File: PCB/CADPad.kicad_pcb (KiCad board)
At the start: 2 copper layers, 30 parts, among them SW1 SW_Push, SW10 RotaryEncoder_Switch, SW2 SW_Push, SW3 SW_Push, SW4 SW_Push, SW5 SW_Push, SW6 SW_Push, SW7 SW_Push, SW8 SW_Push, SW9 SW_Push, U1 XIAO-RP2040-DIP

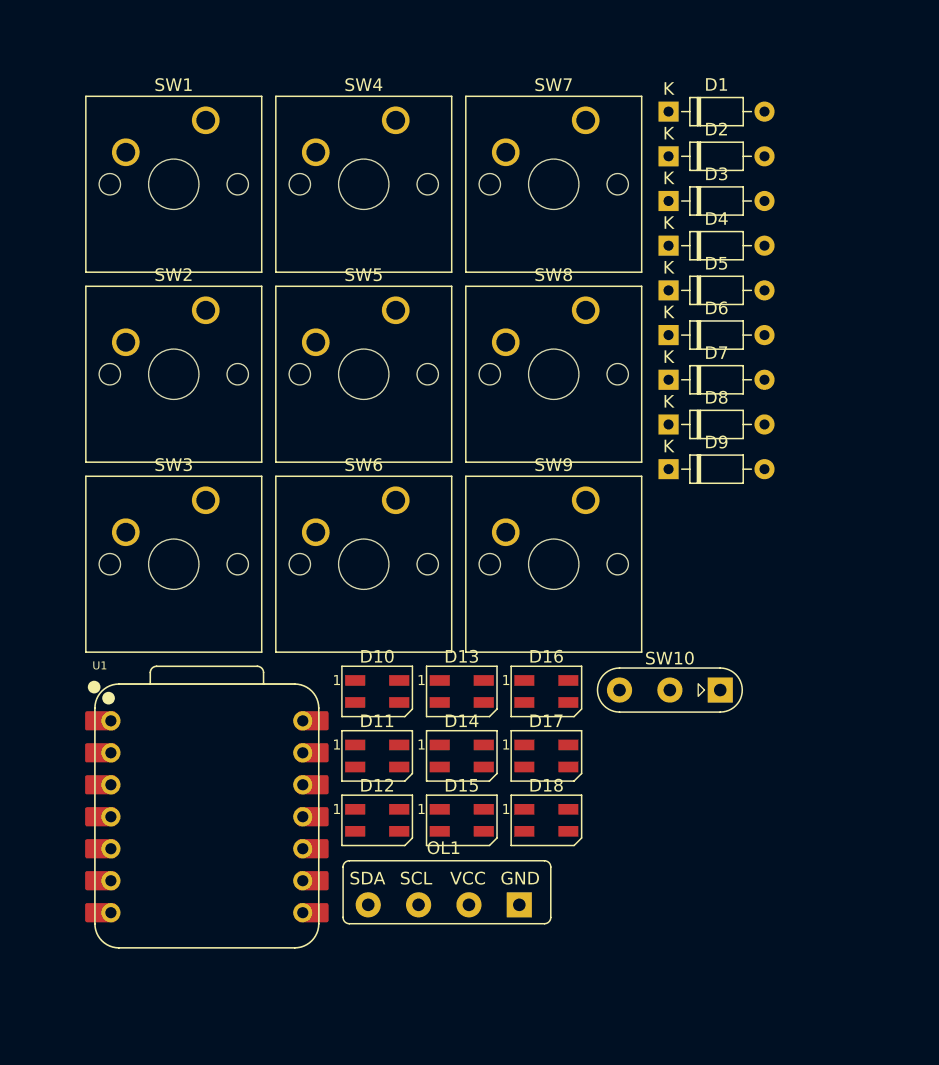
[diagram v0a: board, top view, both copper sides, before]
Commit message: made general layout on pcb
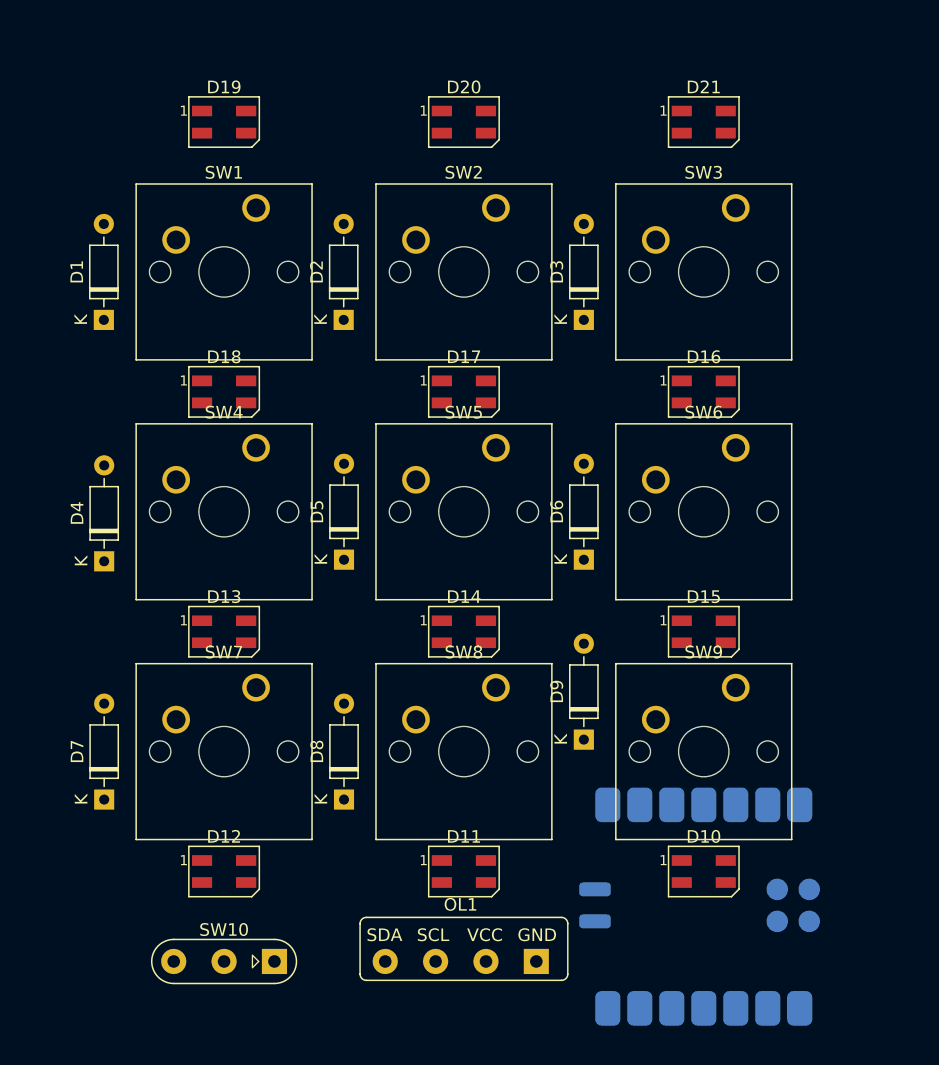
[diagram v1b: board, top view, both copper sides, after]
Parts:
- added D19: SK6812MINI, LED_SMD:LED_SK6812MINI_PLCC4_3.5x3.5mm_P1.75mm, F.Cu at (124.7, 66.2)
- added D20: SK6812MINI, LED_SMD:LED_SK6812MINI_PLCC4_3.5x3.5mm_P1.75mm, F.Cu at (143.8, 66.2)
- added D21: SK6812MINI, LED_SMD:LED_SK6812MINI_PLCC4_3.5x3.5mm_P1.75mm, F.Cu at (162.8, 66.2)
- U1: footprint OPL:XIAO-RP2040-DIP -> OPL:XIAO-RP2040-SMD; moved to B.Cu
- moved D7 55.9 mm to (115.2, 120.0), turned to 90 degrees
- moved SW7 52.1 mm to (127.3, 111.1)
- moved D4 51.4 mm to (115.2, 101.1), turned to 90 degrees
- moved SW3 48.1 mm to (165.4, 73.0)
- moved D1 47.8 mm to (115.2, 81.9), turned to 90 degrees
- moved D18 42.6 mm to (124.7, 87.6)
- moved SW10 41.5 mm to (120.7, 132.9)
- moved U1 40.1 mm to (162.8, 128.6), turned to 90 degrees
- moved D8 39.4 mm to (134.3, 120.0), turned to 90 degrees
- moved D5 33.5 mm to (134.3, 101.0), turned to 90 degrees
- moved SW8 30.8 mm to (146.3, 111.1)
- moved D17 29.6 mm to (143.8, 87.6)
- moved D10 29.6 mm to (162.8, 125.7)
- moved D2 28.9 mm to (134.2, 81.9), turned to 90 degrees
- moved SW4 28.3 mm to (127.3, 92.1)
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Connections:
- D18 pad 1: unconnected-(D18-DOUT-Pad1) -> Net-(D18-DOUT)
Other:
- board text added: "XIAO HERE"

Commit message: traced almost everything
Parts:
- D1, D2, D3, D4, D5, D6, D7, D8, D9: moved to B.Cu
- U1: footprint OPL:XIAO-RP2040-SMD -> OPL:XIAO-RP2040-DIP
- moved D19 59.5 mm to (124.7, 125.7), turned to 180 degrees
- moved D20 59.5 mm to (143.8, 125.7), turned to 180 degrees
- moved D21 59.5 mm to (162.8, 125.7), turned to 180 degrees
- moved D10 57.2 mm to (162.8, 68.6)
- moved D11 57.2 mm to (143.8, 68.6)
- moved D12 57.2 mm to (124.7, 68.6)
- moved U1 56.7 mm to (143.8, 75.2), turned to 180 degrees
- moved D13 19.1 mm to (124.7, 87.6), turned to 180 degrees
- moved D14 19.1 mm to (143.8, 87.6), turned to 180 degrees
- moved D15 19.1 mm to (162.8, 87.6), turned to 180 degrees
- moved D16 19.1 mm to (162.8, 106.7)
- moved D17 19.1 mm to (143.8, 106.7)
- moved D18 19.1 mm to (124.7, 106.7)
- moved OL1 9.85 mm to (147.3, 131.9)
- moved D2 6.85 mm to (130.4, 87.6), turned to 0 degrees
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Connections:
- U1 pad 1: ROW 0 -> LED
- U1 pad 10: COL 0 -> ROW 1
- U1 pad 11: LED -> COL 0
- U1 pad 2: ROW 1 -> COL 2
- U1 pad 3: ROW 2 -> COL 1
- U1 pad 4: EC11 A -> ROW 0
- U1 pad 7: EC11 B -> EC11 A
- U1 pad 8: COL 2 -> EC11 B
- U1 pad 9: COL 1 -> ROW 2
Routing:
- net +5V: track 0.00 -> 259.8 mm, vias 0 -> 2
- net ROW 2: track 0.00 -> 82.0 mm, vias 0 -> 4
- net ROW 1: track 0.00 -> 66.4 mm, vias 0 -> 5
- net EC11 A: track 0.00 -> 61.4 mm
- net SDA: track 0.00 -> 58.3 mm
- net ROW 0: track 0.00 -> 56.2 mm, vias 0 -> 1
- net COL 2: track 0.00 -> 54.9 mm
- net EC11 B: track 0.00 -> 53.1 mm
- net SCL: track 0.00 -> 53.0 mm
- net COL 0: track 0.00 -> 51.7 mm
- net COL 1: track 0.00 -> 45.2 mm
- net Net-(D18-DOUT): track 0.00 -> 24.7 mm, vias 0 -> 2
- net Net-(D15-DOUT): track 0.00 -> 23.2 mm
- net Net-(D12-DOUT): track 0.00 -> 21.6 mm
- net Net-(D14-DOUT): track 0.00 -> 20.2 mm, vias 0 -> 2
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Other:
- board outline added: 61.6 x 70 mm
- board text removed: "XIAO HERE"

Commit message: final board layout?
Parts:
- added REF**: MountingHole_3.2mm_M3_DIN965_Pad, MountingHole:MountingHole_3.2mm_M3_DIN965_Pad, F.Cu at (172.6, 68.8)
- added REF**: MountingHole_3.2mm_M3_DIN965_Pad, MountingHole:MountingHole_3.2mm_M3_DIN965_Pad, F.Cu at (115.0, 131.3)
- added REF**: MountingHole_3.2mm_M3_DIN965_Pad, MountingHole:MountingHole_3.2mm_M3_DIN965_Pad, F.Cu at (115.0, 68.8)
- added REF**: MountingHole_3.2mm_M3_DIN965_Pad, MountingHole:MountingHole_3.2mm_M3_DIN965_Pad, F.Cu at (172.6, 131.3)
- moved D1 1.53 mm to (116.7, 81.9)
- moved D4 1.52 mm to (116.7, 101.1)
- moved D7 1.52 mm to (116.7, 120.0)
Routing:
- net ROW 0: track 56.2 -> 54.6 mm
- net Net-(D1-A): track 6.27 -> 4.74 mm
- net ROW 2: track 82.0 -> 80.4 mm
- net ROW 1: track 66.4 -> 64.9 mm
- net Net-(D7-A): track 6.24 -> 4.72 mm
- net Net-(D4-A): track 6.19 -> 4.66 mm
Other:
- board size 61.6 x 70 mm -> 65.2 x 70 mm
- board text added: "XIAO HERE"

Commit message: arranged everything; before ground pour
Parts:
- moved REF** 3.38 mm to (169.3, 68.0)
- moved REF** 3.38 mm to (118.2, 68.0)
- moved REF** 3.34 mm to (169.3, 130.7)
- moved REF** 3.34 mm to (118.2, 130.7)
- moved OL1 0.50 mm to (147.3, 131.4)
- moved SW10 0.50 mm to (125.7, 131.1)
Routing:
- net Net-(D10-DOUT): track 16.3 -> 46.3 mm, vias 0 -> 2
- net +5V: track 259.8 -> 258.2 mm
- net SDA: track 58.3 -> 57.8 mm
- net SCL: track 53.0 -> 52.5 mm
- net EC11 B: track 53.1 -> 52.6 mm
- net EC11 A: track 61.4 -> 60.9 mm
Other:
- board size 65.2 x 70 mm -> 59.2 x 69.5 mm

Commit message: finished pcb
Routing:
- net GND: track 0.00 -> 2.36 mm, vias 0 -> 139
- net Net-(D10-DOUT): track 46.3 -> 45.5 mm
- added copper zone on B.Cu, net GND
- added copper zone on F.Cu, net GND
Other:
- outline, holes or cut-outs redrawn

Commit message: managed pcb models and started cadding
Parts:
- moved REF** 0.10 mm to (169.3, 68.1)
- moved REF** 0.10 mm to (118.2, 68.1)
- moved REF** 0.10 mm to (118.2, 130.8)
- moved REF** 0.10 mm to (169.3, 130.8)
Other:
- board text added: "CADPad"

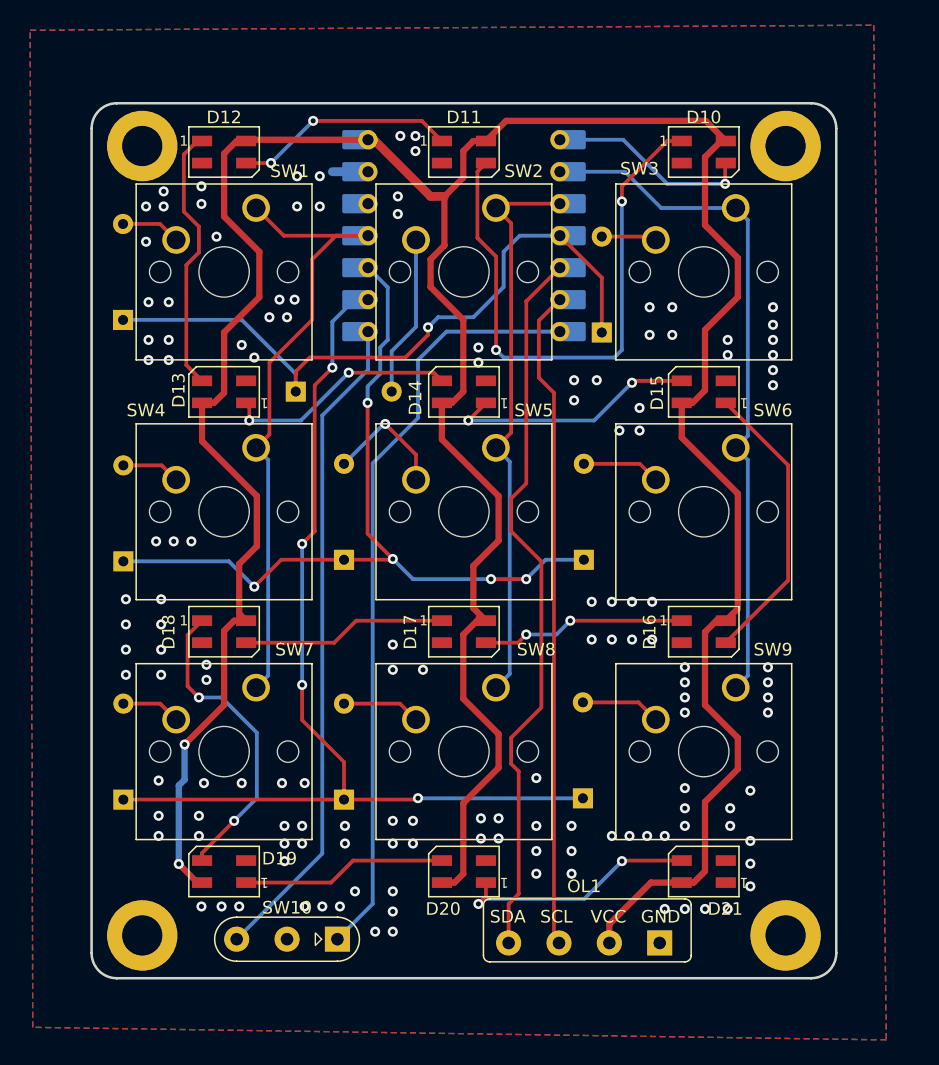
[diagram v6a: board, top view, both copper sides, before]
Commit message: shortened pcb
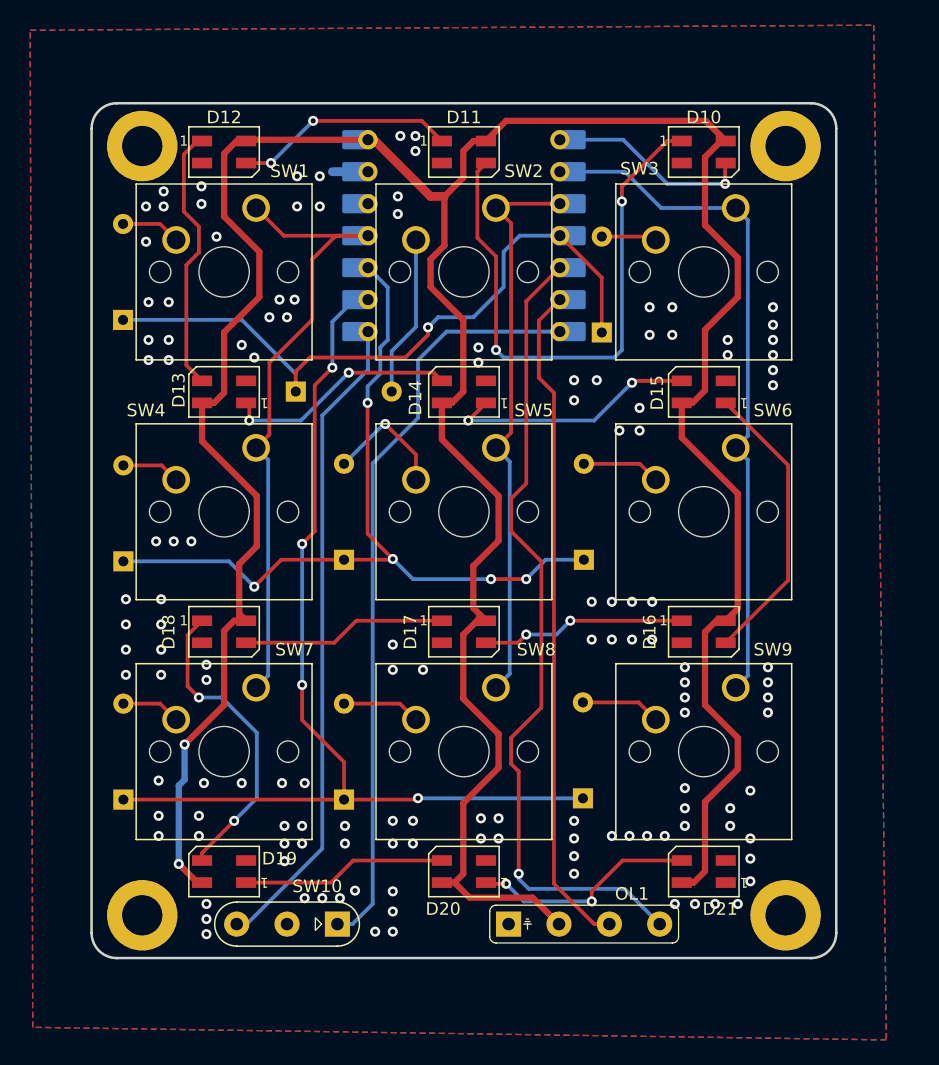
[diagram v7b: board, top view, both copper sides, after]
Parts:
- moved OL1 12.1 mm to (159.3, 129.9), turned to 180 degrees
- moved REF** 1.60 mm to (118.2, 129.2)
- moved REF** 1.60 mm to (169.3, 129.2)
- moved SW10 1.20 mm to (125.7, 129.9)
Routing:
- net SDA: track 57.8 -> 65.1 mm, vias 0 -> 1
- net Net-(D20-DOUT): track 19.5 -> 18.0 mm
- net +5V: track 258.2 -> 259.2 mm
- net SCL: track 52.5 -> 53.3 mm
- net EC11 B: track 52.6 -> 51.8 mm
- net GND: vias 139 -> 136
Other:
- board size 59.2 x 69.5 mm -> 59.2 x 67.9 mm

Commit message: spaced mounting holes farther from switches
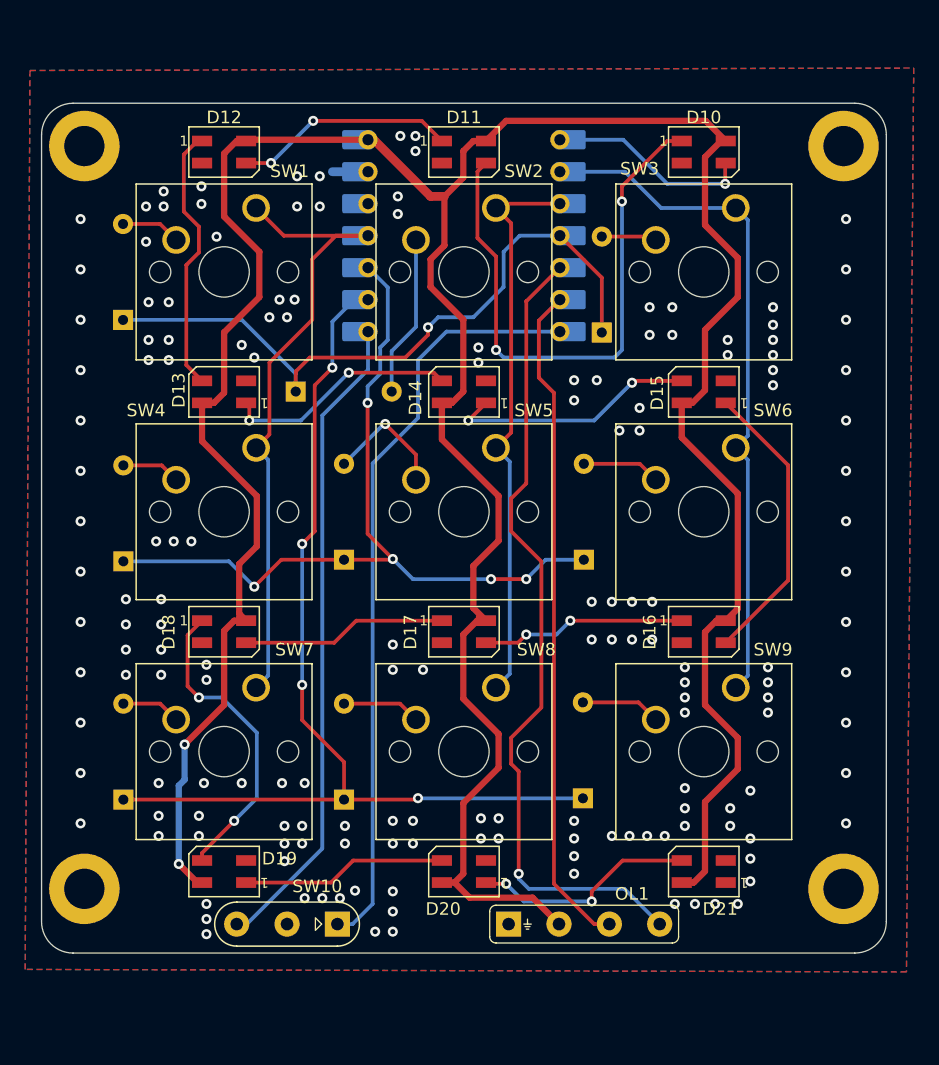
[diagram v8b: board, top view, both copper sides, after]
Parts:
- removed the REF** at (169.3, 68.1)
- removed the REF** at (118.2, 129.2)
- removed the REF** at (118.2, 68.1)
- removed the REF** at (169.3, 129.2)
- added REF**: MountingHole_3.2mm_M3_DIN965_Pad, MountingHole:MountingHole_3.2mm_M3_DIN965_Pad, F.Cu at (113.6, 127.1)
- added REF**: MountingHole_3.2mm_M3_DIN965_Pad, MountingHole:MountingHole_3.2mm_M3_DIN965_Pad, F.Cu at (173.9, 68.1)
- added REF**: MountingHole_3.2mm_M3_DIN965_Pad, MountingHole:MountingHole_3.2mm_M3_DIN965_Pad, F.Cu at (173.9, 127.1)
- added REF**: MountingHole_3.2mm_M3_DIN965_Pad, MountingHole:MountingHole_3.2mm_M3_DIN965_Pad, F.Cu at (113.6, 68.1)
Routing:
- net GND: vias 136 -> 162
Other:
- board size 59.2 x 67.9 mm -> 67.1 x 67.5 mm
